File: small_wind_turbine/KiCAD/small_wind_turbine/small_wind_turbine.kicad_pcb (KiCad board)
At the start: 2 copper layers, 90 x 90 mm, 93 parts, among them J1 Conn_01x03_Male, J2 Conn_01x03_Male, J3 Conn_01x03_Male, K1 G5LE-1, Q1 Q_NMOS_GDS, SW1 SW_Push_SPDT, U10 AZ1117-5.0, U2 UC2844A, U3 LTC4440ES6, U4 Opamp_Quad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

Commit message: finalize relative positions; ready to start finessing
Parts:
- removed TP7: TestPoint_2Pole, small_wind_turbine:Oscilloscope_Test_Point
- Jbat1, Jres1: footprint TerminalBlock_Phoenix:TerminalBlock_Phoenix_MKDS-1,5-2-5.08_1x02_P5.08mm_Horizontal -> small_wind_turbine:TerminalBlock_1x02_P5.08mm_leads
- Jgen1: footprint TerminalBlock_Phoenix:TerminalBlock_Phoenix_MKDS-1,5-3-5.08_1x03_P5.08mm_Horizontal -> small_wind_turbine:TerminalBlock_1x03_P5.08mm_Horizontal
- moved D11 40.7 mm to (105.5, 111.8), turned to 180 degrees
- moved D8 40.5 mm to (105.5, 102.8), turned to 180 degrees
- moved D10 39.7 mm to (105.5, 108.8), turned to 180 degrees
- moved D9 39.7 mm to (105.5, 105.8), turned to 180 degrees
- moved R14 32.9 mm to (101.6, 102.8), turned to 0 degrees
- moved R17 32.9 mm to (101.5, 111.8), turned to 0 degrees
- moved R16 31.8 mm to (101.5, 108.8), turned to 0 degrees
- moved R15 31.7 mm to (101.5, 105.8), turned to 0 degrees
- moved R10 30.4 mm to (50.6, 114.1)
- moved R11 30.4 mm to (53.2, 114.1)
- moved A1 30.4 mm to (88.7, 97.2)
- moved TP9 11.2 mm to (50.4, 73.3), turned to 90 degrees
- moved C14 2.69 mm to (46.3, 69.8)
- moved C15 2.69 mm to (46.3, 71.8)
- moved C16 2.69 mm to (46.3, 73.8)
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
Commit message: finish finessing placement
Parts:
- moved TP10 12.6 mm to (84.6, 89.8), turned to -90 degrees
- moved TP3 2.81 mm to (88.1, 89.8), turned to -90 degrees
- moved D12 1.93 mm to (105.5, 34.9)
- moved R18 1.93 mm to (101.3, 34.9)
- moved R13 1.50 mm to (47.5, 84.1)
- moved D7 1.50 mm to (47.5, 86.1)
- moved U10 1.50 mm to (46.9, 78.4)
- moved Rf1 1.26 mm to (72.2, 86.7)
- moved C14 1.19 mm to (46.9, 68.8)
- moved C15 1.19 mm to (46.9, 70.8)
- moved C16 1.19 mm to (46.9, 72.8)
- moved TP9 1.14 mm to (50.6, 72.2)
- moved C10 0.84 mm to (61.3, 71.6)
- moved Q1 0.80 mm to (126.8, 57.2)
- moved R1 0.80 mm to (126.8, 60.3)
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
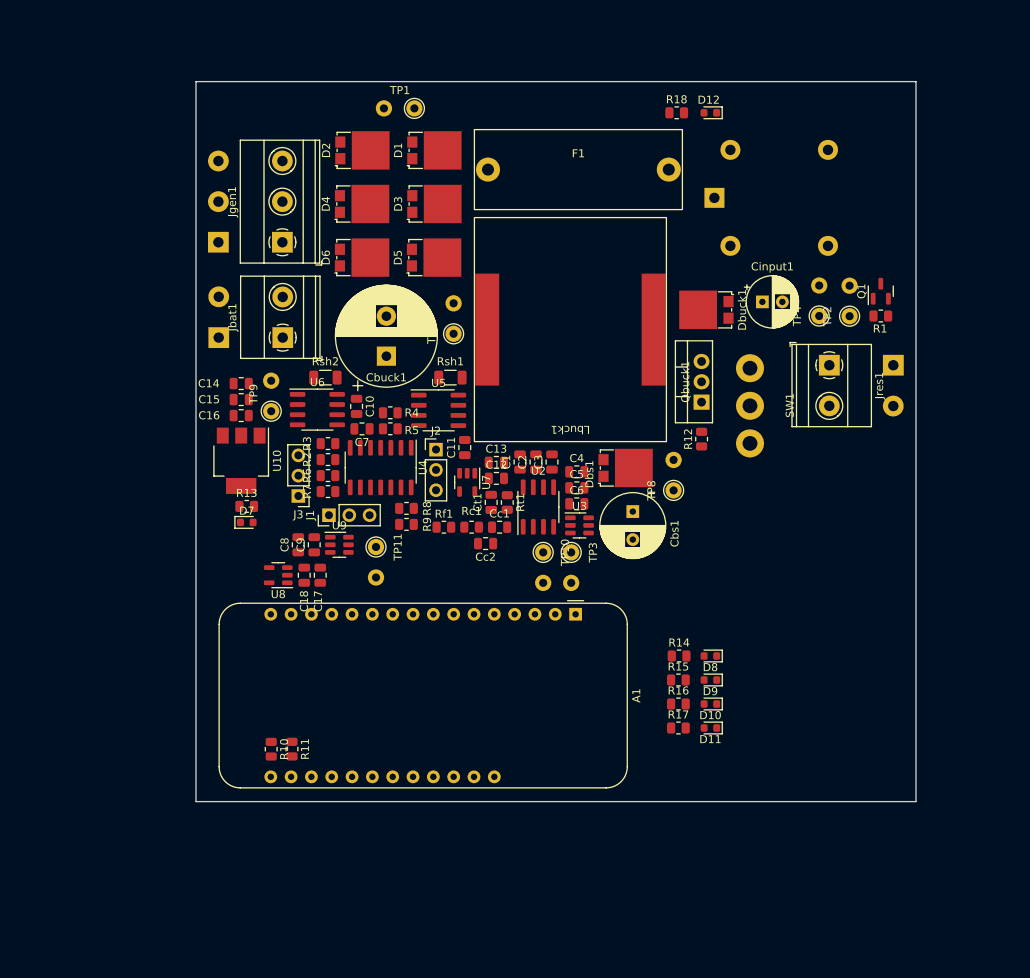
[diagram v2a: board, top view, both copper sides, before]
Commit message: wip laying traces
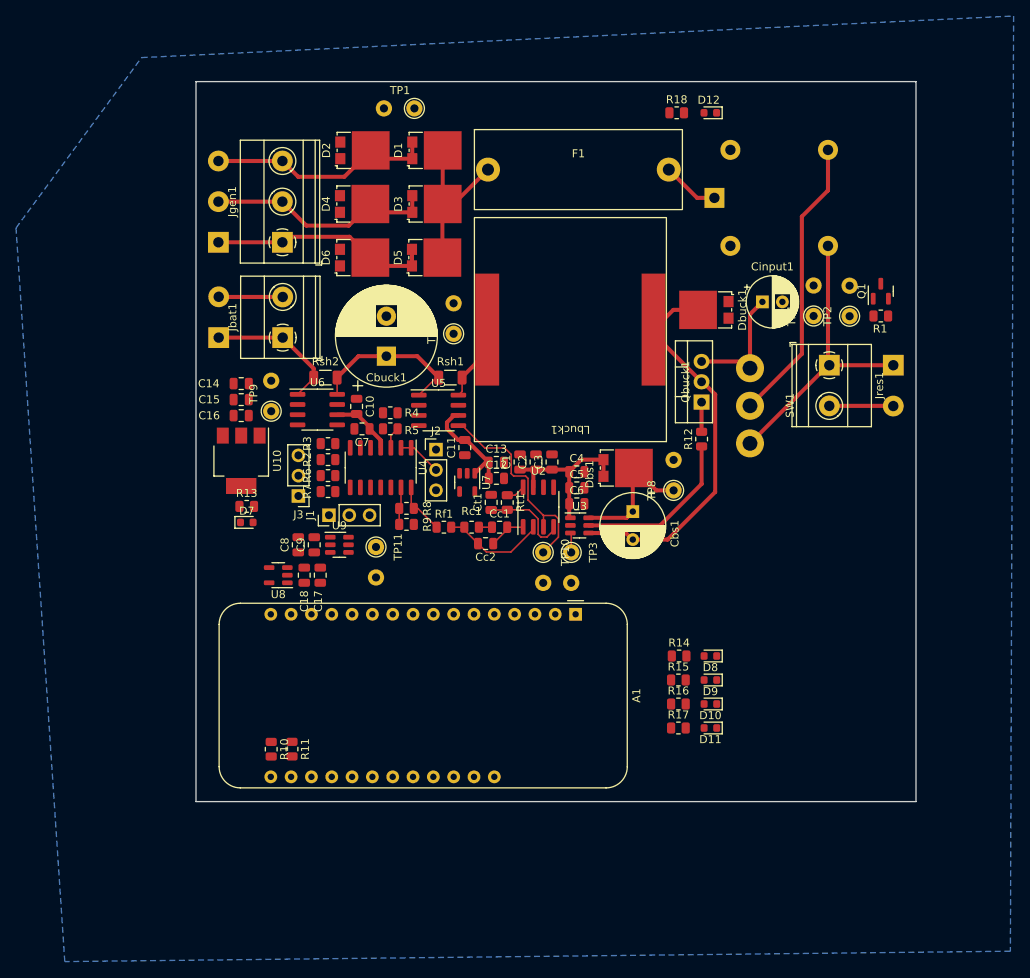
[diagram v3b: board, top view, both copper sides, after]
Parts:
- moved TP4 0.70 mm to (118.4, 60.3)
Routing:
- net /GATE_SOURCE: track 0.00 -> 48.8 mm
- net +12V: track 0.00 -> 41.8 mm
- net Net-(Jres1-Pad1): track 0.00 -> 36.9 mm
- net Net-(K1-Pad3): track 0.00 -> 36.0 mm
- net Net-(D3-Pad2): track 0.00 -> 29.1 mm
- net Net-(D1-Pad2): track 0.00 -> 28.9 mm
- net Net-(D5-Pad2): track 0.00 -> 28.1 mm
- net /UC2844_ISENSE: track 0.00 -> 26.8 mm
- net +5V: track 0.00 -> 21.8 mm
- net Net-(R12-Pad1): track 0.00 -> 21.0 mm
- net Net-(D1-Pad1): track 0.00 -> 20.9 mm
- net /BATTERY_POSITIVE: track 0.00 -> 17.5 mm
- net Net-(Cbs1-Pad1): track 0.00 -> 17.5 mm
- net GND: track 0.00 -> 16.0 mm
- net /RECTIFIER_VDD: track 0.00 -> 15.3 mm
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- added copper zone on B.Cu, net GND

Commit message: wip laying traces (2)
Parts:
- turned R5 to 0 degrees
- turned R4 to 180 degrees
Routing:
- net +12V: track 41.8 -> 139.5 mm
- net GND: track 16.0 -> 75.1 mm
- net Net-(K1-Pad5): track 0.00 -> 40.9 mm
- net +5V: track 21.8 -> 42.1 mm
- net Net-(TP9-Pad1): track 0.00 -> 15.4 mm
- net Net-(J3-Pad2): track 0.00 -> 11.9 mm
- net Net-(R6-Pad1): track 0.00 -> 9.76 mm
- net Net-(J3-Pad1): track 0.00 -> 9.52 mm
- net /UC2844_GATE_OUTPUT: track 2.46 -> 9.92 mm
- net /RECTIFIER_LED: track 7.16 -> 14.3 mm
- net Net-(D1-Pad1): track 20.9 -> 27.6 mm
- net Net-(R2-Pad1): track 0.00 -> 5.95 mm
- net Net-(J1-Pad2): track 0.00 -> 4.79 mm
- net Net-(J1-Pad1): track 0.00 -> 2.82 mm
- net Net-(D12-Pad2): track 0.00 -> 2.50 mm
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
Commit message: almost finished laying traces
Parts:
- moved C7 1.55 mm to (63.2, 73.5), turned to 90 degrees
- moved R4 0.41 mm to (65.9, 72.4)
- moved R5 0.41 mm to (65.9, 74.4)
- moved C11 0.41 mm to (74.4, 76.7)
- moved C10 0.13 mm to (61.2, 71.7)
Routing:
- net +5V: track 42.1 -> 102.9 mm, vias 0 -> 4
- net GND: track 75.1 -> 117.8 mm, vias 0 -> 19
- net /GATE_SOURCE: track 48.8 -> 68.8 mm, vias 0 -> 1
- net +12V: track 139.5 -> 158.9 mm, vias 0 -> 2
- net /RECTIFIER_VDD: track 15.3 -> 28.4 mm, vias 0 -> 2
- net /BATTERY_POSITIVE: track 17.5 -> 30.3 mm, vias 0 -> 2
- net Net-(J1-Pad2): track 4.79 -> 10.2 mm
- net Net-(J2-Pad1): track 0.00 -> 4.18 mm
- net Net-(J3-Pad2): track 11.9 -> 13.7 mm

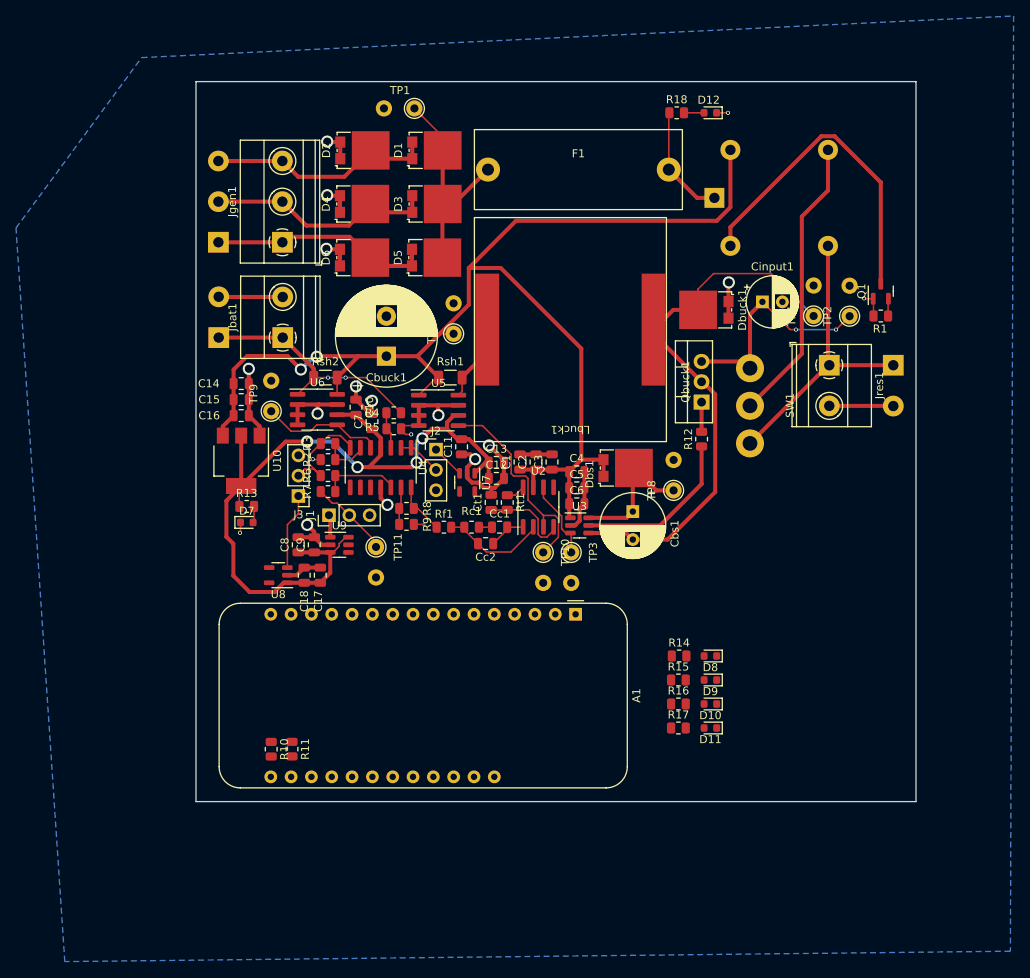
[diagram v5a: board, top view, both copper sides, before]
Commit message: finish laying traces
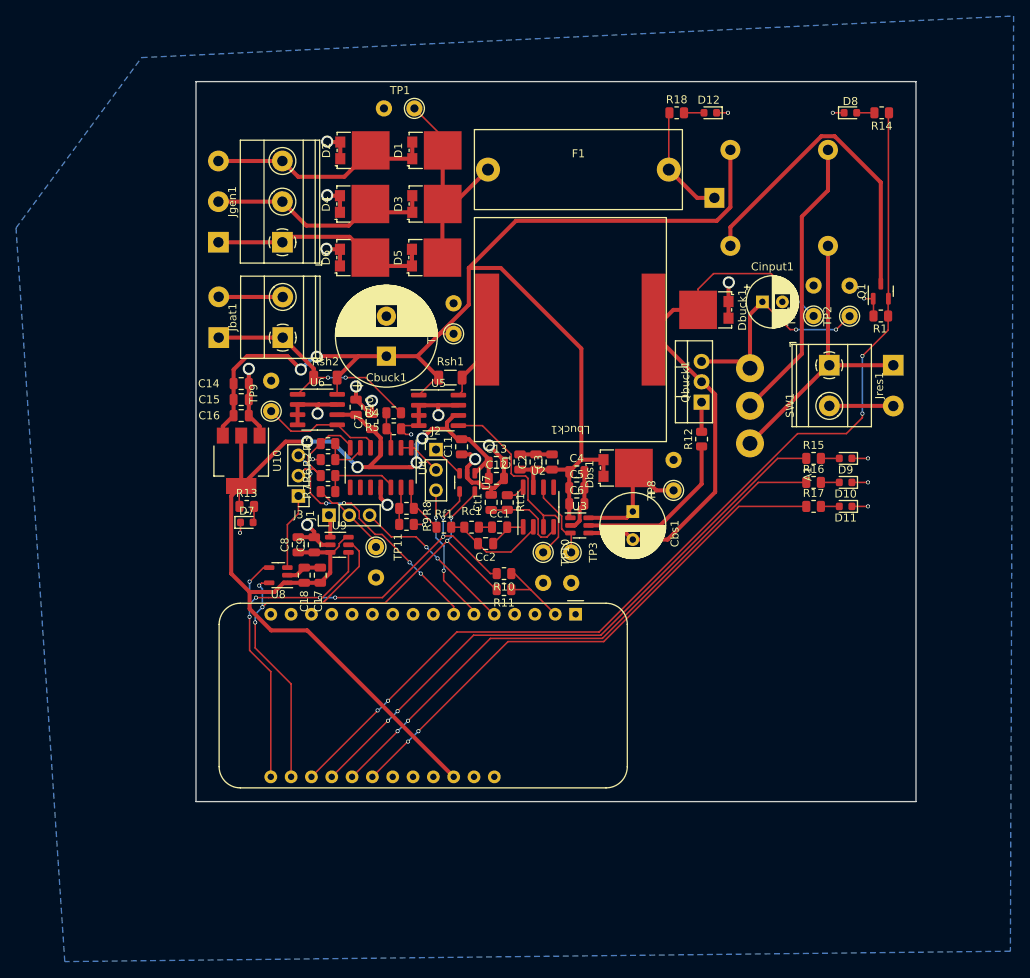
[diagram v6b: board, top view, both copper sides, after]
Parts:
- moved R14 72.5 mm to (126.9, 34.9), turned to 180 degrees
- moved D8 70.1 mm to (123.0, 34.9), turned to 0 degrees
- moved R10 36.5 mm to (79.7, 92.5), turned to 180 degrees
- moved R11 33.2 mm to (79.7, 94.5), turned to 180 degrees
- moved D10 32.4 mm to (122.4, 81.1)
- moved D11 32.4 mm to (122.4, 84.1)
- moved D9 32.4 mm to (122.4, 78.1)
- moved R15 32.4 mm to (118.4, 78.1)
- moved R16 32.4 mm to (118.4, 81.1)
- moved R17 32.4 mm to (118.4, 84.1)
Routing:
- net /RELAY_DRIVE: track 2.18 -> 127.0 mm, vias 0 -> 4
- net /WEMOS_SCL: track 0.00 -> 82.1 mm, vias 0 -> 5
- net /WEMOS_SDA: track 0.00 -> 78.9 mm, vias 0 -> 7
- net /GPIO_LED1: track 0.00 -> 75.8 mm, vias 0 -> 2
- net /GPIO_LED2: track 0.00 -> 72.0 mm, vias 0 -> 2
- net /GPIO_LED3: track 0.00 -> 68.2 mm, vias 0 -> 2
- net +5V: track 102.9 -> 138.7 mm
- net /ALTERNATE_ADC_2: track 0.00 -> 30.7 mm, vias 0 -> 5
- net /ALTERNATE_DAC: track 0.00 -> 20.7 mm, vias 0 -> 2
- net /ALTERNATE_ADC: track 0.00 -> 17.5 mm, vias 0 -> 2
- net +3V3: track 0.00 -> 10.0 mm
- net GND: track 117.8 -> 125.2 mm, vias 19 -> 23
- net Net-(D9-Pad2): track 0.00 -> 2.30 mm
- net Net-(D11-Pad2): track 0.00 -> 2.30 mm
- net Net-(D10-Pad2): track 0.00 -> 2.30 mm
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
